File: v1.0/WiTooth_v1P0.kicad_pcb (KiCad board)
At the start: 4 copper layers, 67 x 25.8 mm, 80 parts, among them P1 USB_A_MALE, P4 CONN_01X20, P5 CONN_01X20, Q1 2N3904-MMBT, Q2 2N3904-MMBT, SW1 RESET, SW2 BOOT, SW3 USER_SW, U1 AMS1117-3V3, U2 CP2102, U3 ESP-32_WROOM32_Rectangle, Y1 Crystal

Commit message: Added images folder; schematic verified
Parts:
- added REF**: VIA_0.5mm, via:VIA_0.5mm, F.Cu at (149.7, 95.3)
- moved REF** 0.48 mm to (123.7, 106.9)
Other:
- board text added: "67 x 25.8 mm"

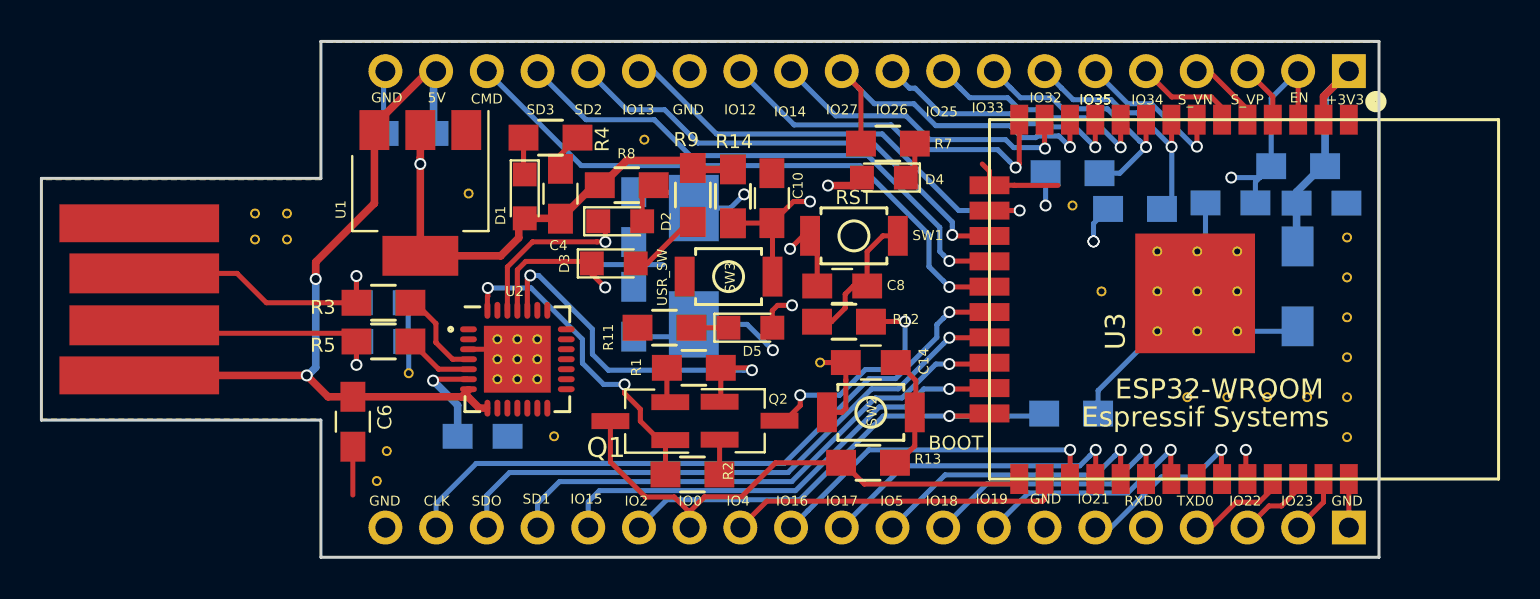
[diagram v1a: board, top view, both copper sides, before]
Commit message: BOM verified
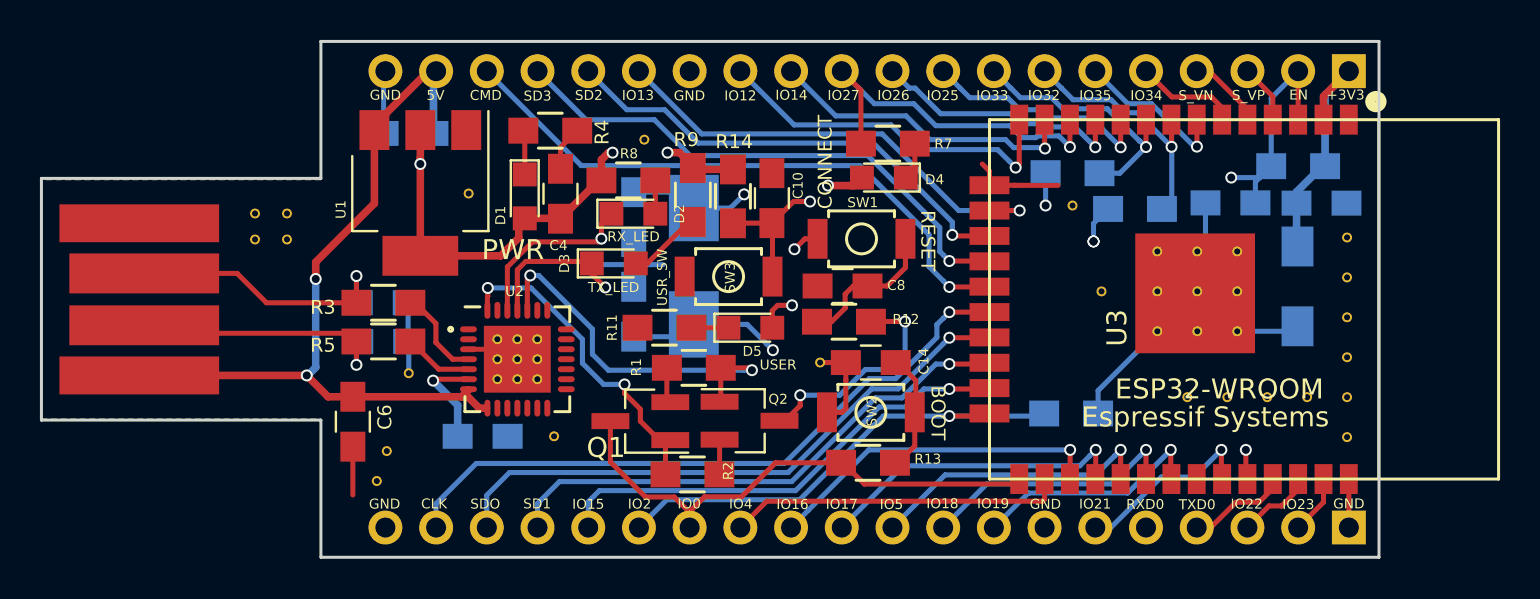
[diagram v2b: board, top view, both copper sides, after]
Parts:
- D1: value PWR_GREEN -> PWR
- D2: value YELLOW -> RX_LED
- D3: value YELLOW -> TX_LED
- D4: value CONN_LED -> CONNECT
- D5: value USER_LED -> USER
- Y1: value Crystal -> 32.768 KHz Crystal
- moved D2 0.76 mm to (127.7, 95.7)
- moved SW1 0.41 mm to (139.1, 97.0)
- moved R4 0.35 mm to (123.5, 91.5)
- moved R8 0.25 mm to (127.4, 94.0)
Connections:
- U2 pad 1: Net-(U2-Pad1) -> (no net)
- U2 pad 10: Net-(U2-Pad10) -> (no net)
- U2 pad 11: Net-(U2-Pad11) -> (no net)
- U2 pad 12: Net-(U2-Pad12) -> (no net)
- U2 pad 13: Net-(U2-Pad13) -> (no net)
- U2 pad 14: Net-(U2-Pad14) -> (no net)
- U2 pad 15: Net-(U2-Pad15) -> (no net)
- U2 pad 16: Net-(U2-Pad16) -> (no net)
- U2 pad 17: Net-(U2-Pad17) -> (no net)
- U2 pad 18: Net-(U2-Pad18) -> (no net)
- U2 pad 19: Net-(U2-Pad19) -> (no net)
- U2 pad 2: Net-(U2-Pad2) -> (no net)
- U2 pad 20: Net-(U2-Pad20) -> (no net)
- U2 pad 21: Net-(U2-Pad21) -> (no net)
- U2 pad 22: Net-(U2-Pad22) -> (no net)
- U2 pad 23: Net-(U2-Pad23) -> (no net)
- U2 pad 27: Net-(U2-Pad27) -> (no net)
- U2 pad 9: Net-(U2-Pad9) -> (no net)
- U3 pad 32: Net-(U3-Pad32) -> (no net)
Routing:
- net GND: track 49.8 -> 47.6 mm
- net +3V3: track 39.3 -> 37.4 mm, vias 2 -> 4
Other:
- board text added: "RESET"
- board text removed: "RST"

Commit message: updated the 2N3904 npn transistor footprint
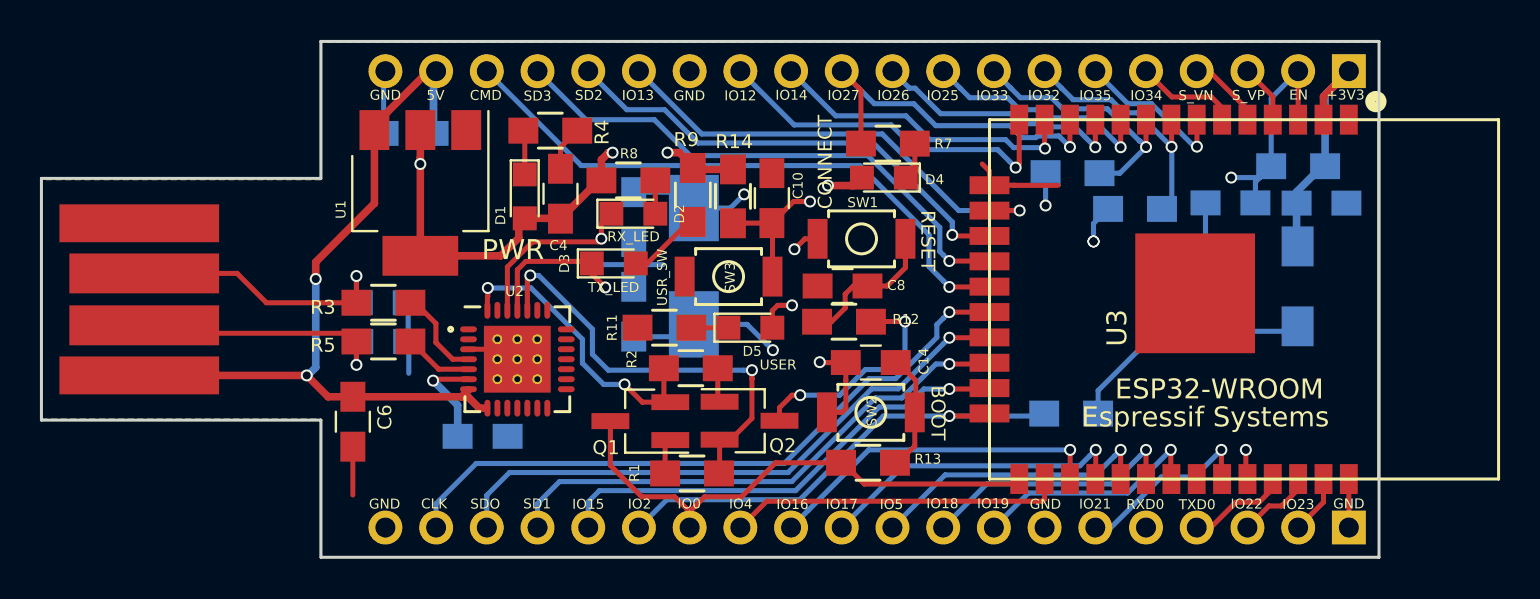
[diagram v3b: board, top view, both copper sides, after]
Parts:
- removed G***: LOGO, logos:thingTronics_10mm
- removed the REF** at (149.7, 95.3)
- removed the REF** at (159.4, 104.9)
- removed the REF** at (161.4, 104.9)
- removed the REF** at (163.4, 106.9)
- removed the REF** at (163.4, 104.9)
- removed the REF** at (163.4, 102.9)
- removed the REF** at (163.4, 100.9)
- removed the REF** at (163.4, 98.9)
- removed the REF** at (163.4, 96.9)
- removed the REF** at (151.1, 99.6)
- removed the REF** at (115.3, 107.6)
- removed the REF** at (116.4, 103.7)
- removed the REF** at (114.8, 109.1)
- removed the REF** at (119.4, 94.7)
- removed the REF** at (157.9, 101.6)
- removed the REF** at (155.9, 101.6)
- removed the REF** at (153.9, 101.6)
- removed the REF** at (157.9, 99.6)
- removed the REF** at (155.9, 99.6)
- removed the REF** at (153.9, 99.6)
- removed the REF** at (157.9, 97.6)
- removed the REF** at (155.9, 97.6)
- removed the REF** at (110.3, 97.0)
- removed the REF** at (153.9, 97.6)
- removed the REF** at (128.2, 92.0)
- removed the REF** at (110.3, 95.7)
- removed the REF** at (108.7, 97.0)
- removed the REF** at (108.7, 95.7)
- removed the REF** at (137.0, 103.2)
- removed the REF** at (123.7, 106.9)
- removed the REF** at (155.4, 104.9)
- removed the REF** at (157.4, 104.9)
- Q1, Q2: value 2N3904-MMBT -> MMBT3904
- Y1: value 32.768 KHz Crystal -> Crystal
- moved R2 5.32 mm to (130.5, 103.5)
- moved R1 5.29 mm to (130.6, 108.7)
- moved REF** 0.16 mm to (57.6, 86.7)
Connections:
- Q1 pad 1: DTR -> Net-(Q1-Pad1)
- Q1 pad 2: Net-(Q1-Pad2) -> DTR
- Q2 pad 1: RTS -> Net-(Q2-Pad1)
- Q2 pad 2: Net-(Q2-Pad2) -> RTS
- R1 pad 1: Net-(Q1-Pad2) -> Net-(Q1-Pad1)
- R2 pad 1: Net-(Q2-Pad2) -> Net-(Q2-Pad1)
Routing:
- net RTS: track 19.0 -> 22.0 mm
- net Net-(Q1-Pad1): track 0.00 -> 2.12 mm
- net Net-(Q1-Pad2): track 2.12 -> 0.00 mm
- net Net-(Q2-Pad2): track 1.74 -> 0.00 mm
- net Net-(Q2-Pad1): track 0.00 -> 1.72 mm
- net DTR: track 16.8 -> 15.2 mm
- net IO0: track 26.8 -> 26.1 mm
- net GND: vias 1 -> 2
